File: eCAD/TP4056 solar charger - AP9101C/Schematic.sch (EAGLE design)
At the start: 33 parts, among them IC1 TP4056X, IC2 AP9101CK6-ADTRG1, IC3 FDS6898A, Q1 SI2347DS-T1-GE3, X1 PV_PANEL, X2 BATTERY, X3 OUTPUT

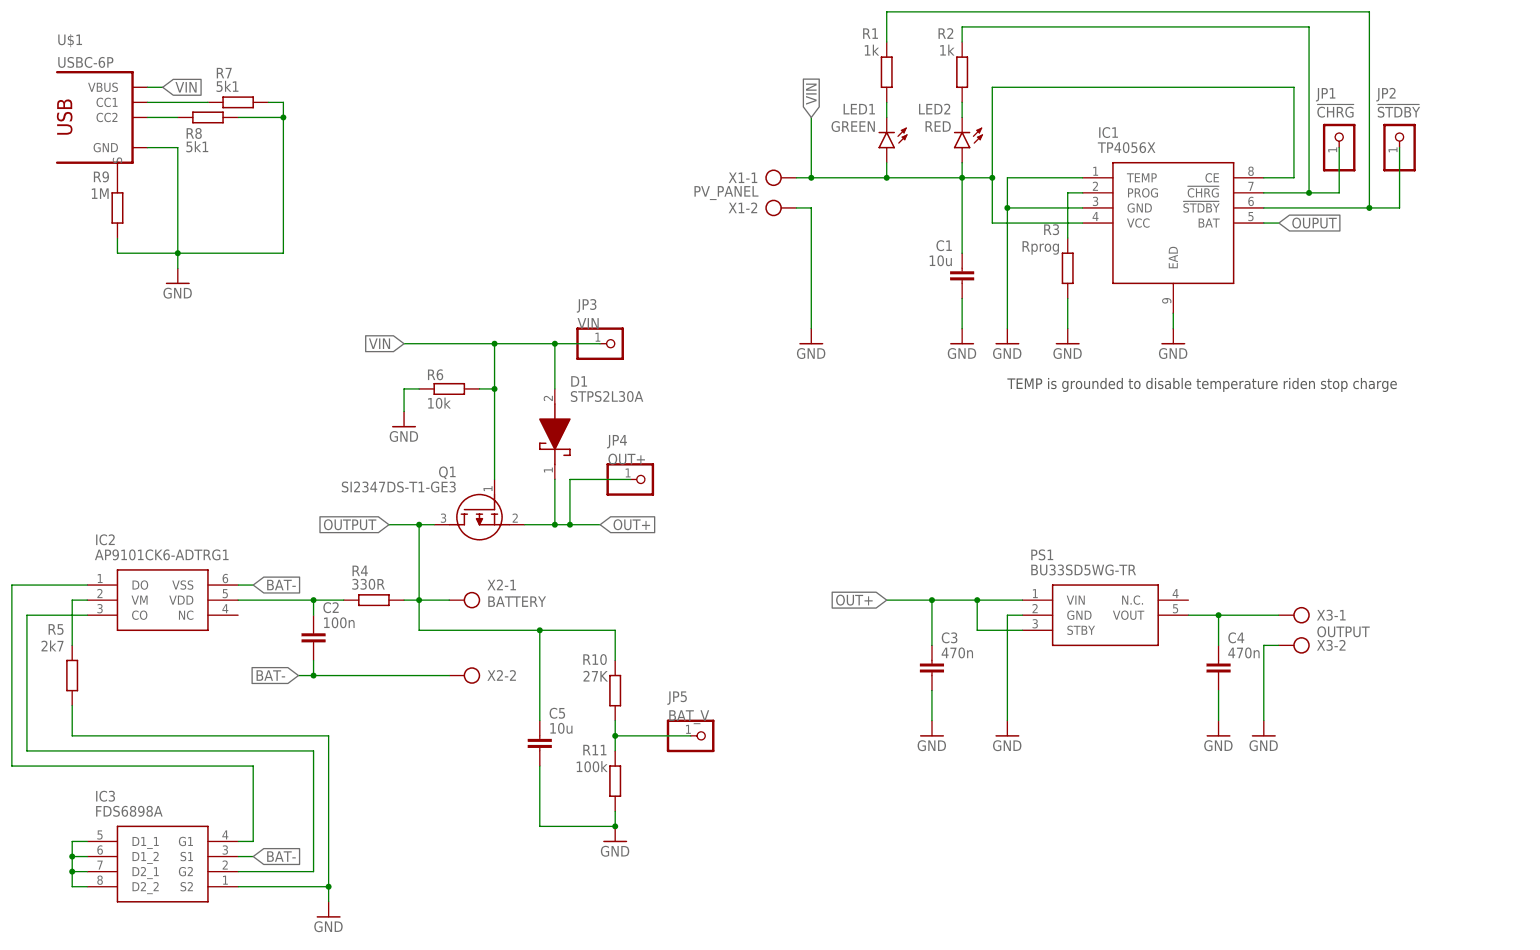
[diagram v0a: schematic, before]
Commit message: RTC example and test
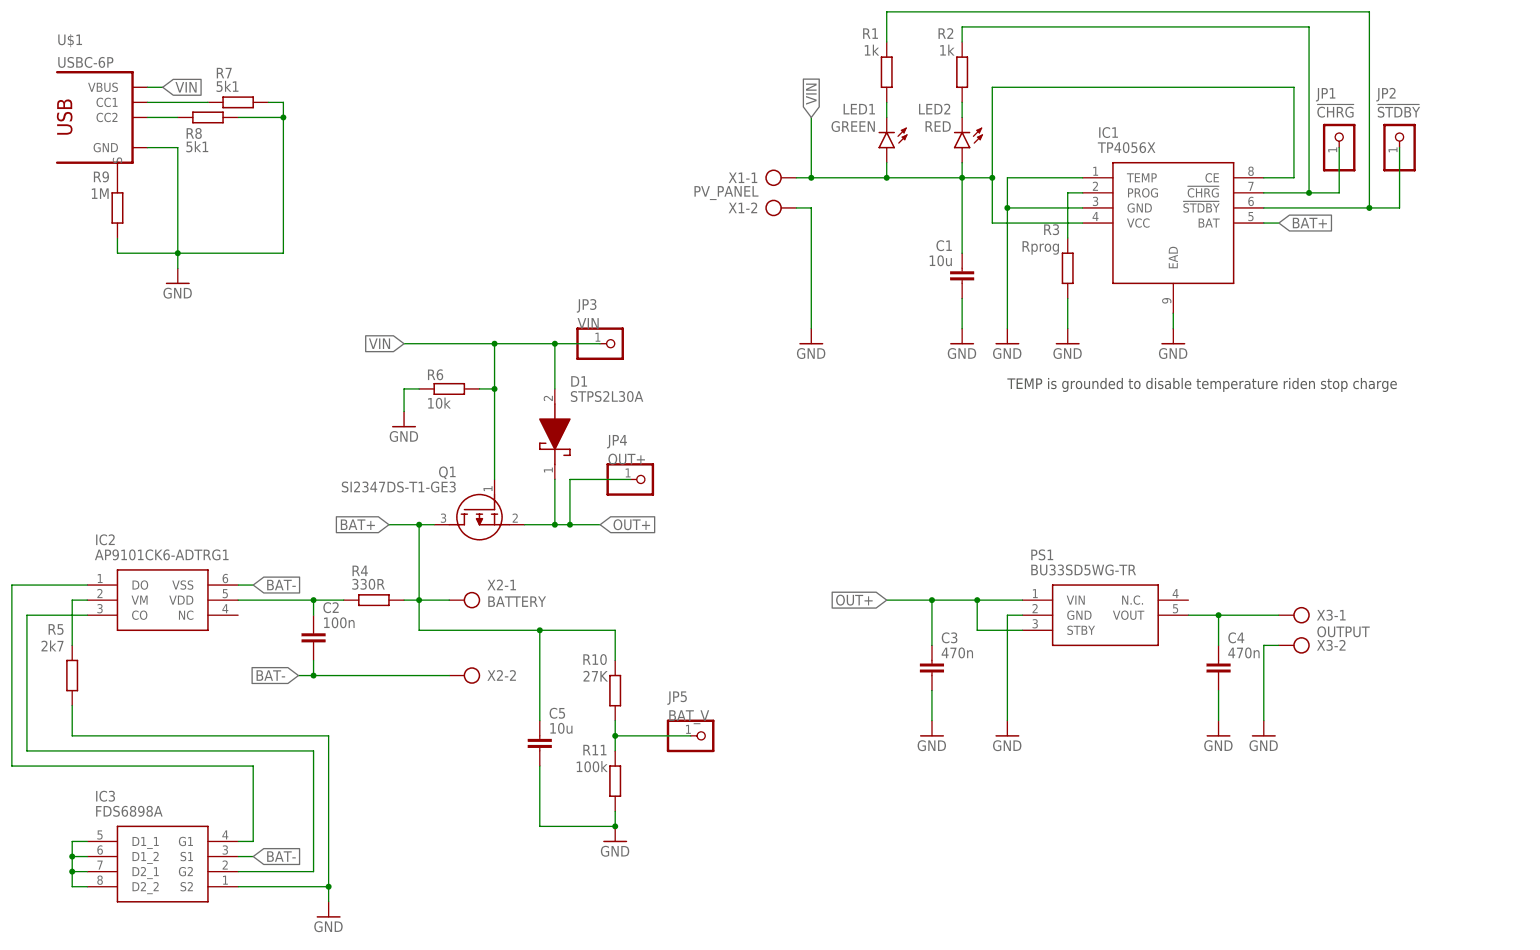
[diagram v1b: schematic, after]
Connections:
- net N$14 renamed VOUT
- removed net OUPUT: IC1.BAT
- removed net OUTPUT: C5.1, Q1.D, R10.2, R4.2, X2-1.KL
- new net BAT+: C5.1, IC1.BAT, Q1.D, R10.2, R4.2, X2-1.KL
